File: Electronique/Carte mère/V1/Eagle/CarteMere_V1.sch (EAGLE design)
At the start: 25 parts, among them J100 BP_Rouge, J101 BP Jaune, J102 BP Vert, J600 LED_VERTE, J601 LED_JAUNE, J602 LED_ROUGE, Q500 SI2303DS, Q501 SI2302DS, U200 FIREBEETLE-ESP32-DFR0478, U300 RTC_ADA-3295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

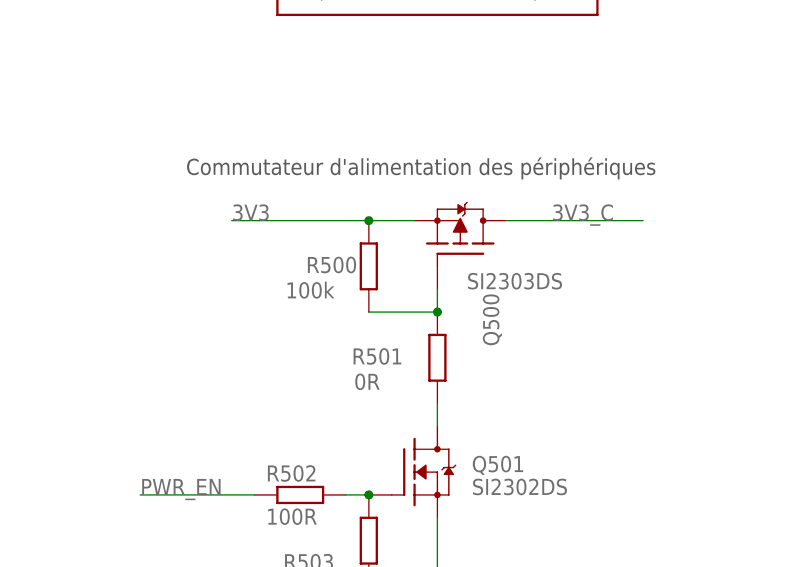
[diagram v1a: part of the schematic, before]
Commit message: Modificaiton du diamètre perçage vis et recréation des fichiers gerbers
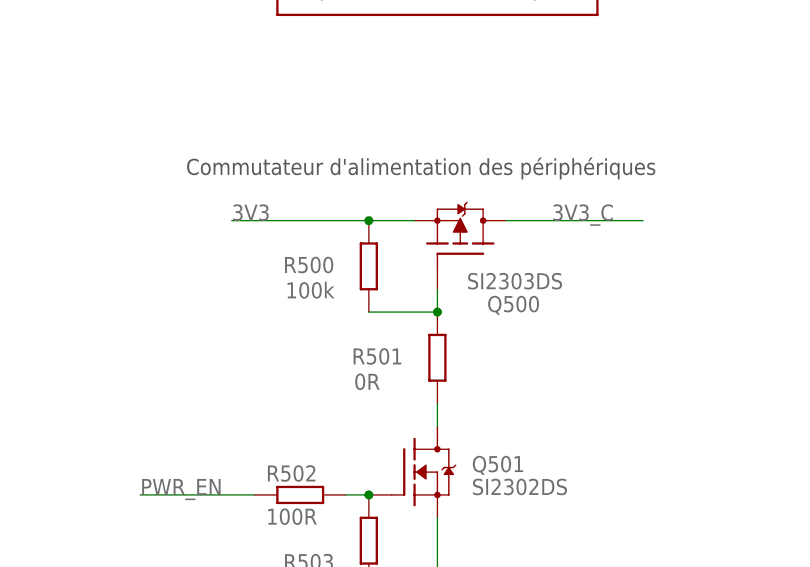
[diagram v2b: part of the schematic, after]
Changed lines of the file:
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@@
 <part name="SUPPLY3" library="supply2" library_urn="urn:adsk.eagle:library:372" deviceset="GND" device=""/>
 <part name="SUPPLY4" library="supply2" library_urn="urn:adsk.eagle:library:372" deviceset="GND" device=""/>
-<part name="R501" library="Eagle_UOF_Lib" deviceset="R_1/4W" device="10" value="0R"/>
-<part name="R500" library="Eagle_UOF_Lib" deviceset="R_1/4W" device="10" value="100k"/>
 <part name="Q500" library="Eagle_UOF_Lib" deviceset="SI2303DS" device=""/>
 <part name="JTEST300" library="pinhead" library_urn="urn:adsk.eagle:library:325" deviceset="PINHD-1X1" device="" package3d_urn="urn:adsk.eagle:package:22485/1"/>
@@
 <part name="JTEST400" library="pinhead" library_urn="urn:adsk.eagle:library:325" deviceset="PINHD-1X1" device="" package3d_urn="urn:adsk.eagle:package:22485/1"/>
 <part name="JTEST401" library="pinhead" library_urn="urn:adsk.eagle:library:325" deviceset="PINHD-1X1" device="" package3d_urn="urn:adsk.eagle:package:22485/1"/>
+<part name="R501" library="Eagle_UOF_Lib" deviceset="R_1/4W" device="10" value="0R"/>
+<part name="R500" library="Eagle_UOF_Lib" deviceset="R_1/4W" device="10" value="100k"/>
 </parts>
 <sheets>
@@
 <instance part="SUPPLY3" gate="GND" x="137.16" y="20.32"/>
 <instance part="SUPPLY4" gate="GND" x="137.16" y="5.08"/>
-<instance part="R501" gate="G$1" x="73.66" y="0" smashed="yes" rot="R90">
-<attribute name="NAME" x="69.85" y="1.0414" size="1.778" layer="95" rot="R180"/>
-<attribute name="VALUE" x="67.31" y="-1.778" size="1.778" layer="96" rot="R180"/>
-</instance>
-<instance part="R500" gate="G$1" x="66.04" y="10.16" smashed="yes" rot="R90">
-<attribute name="NAME" x="64.77" y="11.2014" size="1.778" layer="95" rot="R180"/>
-<attribute name="VALUE" x="62.23" y="8.382" size="1.778" layer="96" rot="R180"/>
-</instance>
 <instance part="Q500" gate="G$1" x="76.2" y="12.7" smashed="yes" rot="MR90">
 <attribute name="VALUE" x="87.63" y="7.62" size="1.778" layer="96" rot="MR0"/>
-<attribute name="NAME" x="78.74" y="1.27" size="1.778" layer="95" rot="MR90"/>
+<attribute name="NAME" x="85.09" y="5.08" size="1.778" layer="95" rot="MR0"/>
 </instance>
 <instance part="JTEST300" gate="G$1" x="17.78" y="-25.4" rot="R90"/>
@@
 <instance part="JTEST400" gate="G$1" x="132.08" y="86.36" rot="R90"/>
 <instance part="JTEST401" gate="G$1" x="124.46" y="86.36" rot="R90"/>
+<instance part="R501" gate="G$1" x="73.66" y="0" smashed="yes" rot="R90">
+<attribute name="NAME" x="69.85" y="1.0414" size="1.778" layer="95" rot="R180"/>
+<attribute name="VALUE" x="67.31" y="-1.778" size="1.778" layer="96" rot="R180"/>
+</instance>
+<instance part="R500" gate="G$1" x="66.04" y="10.16" smashed="yes" rot="R90">
+<attribute name="NAME" x="62.23" y="11.2014" size="1.778" layer="95" rot="R180"/>
+<attribute name="VALUE" x="62.23" y="8.382" size="1.778" layer="96" rot="R180"/>
+</instance>
 </instances>
 <busses>
@@
 </segment>
 <segment>
+<wire x1="71.12" y1="15.24" x2="66.04" y2="15.24" width="0.1524" layer="91"/>
+<label x="50.8" y="15.24" size="1.778" layer="95"/>
+<pinref part="Q500" gate="G$1" pin="S"/>
 <pinref part="R500" gate="G$1" pin="2"/>
 <wire x1="66.04" y1="15.24" x2="50.8" y2="15.24" width="0.1524" layer="91"/>
-<label x="50.8" y="15.24" size="1.778" layer="95"/>
-<pinref part="Q500" gate="G$1" pin="S"/>
-<wire x1="66.04" y1="15.24" x2="71.12" y2="15.24" width="0.1524" layer="91"/>
 <junction x="66.04" y="15.24"/>
 </segment>
@@
 <net name="N$7" class="0">
 <segment>
-<pinref part="R501" gate="G$1" pin="2"/>
-<pinref part="R500" gate="G$1" pin="1"/>
 <wire x1="66.04" y1="5.08" x2="73.66" y2="5.08" width="0.1524" layer="91"/>
 <pinref part="Q500" gate="G$1" pin="G"/>
 <wire x1="73.66" y1="7.62" x2="73.66" y2="5.08" width="0.1524" layer="91"/>
+<pinref part="R501" gate="G$1" pin="2"/>
 <junction x="73.66" y="5.08"/>
-</segment>
-</net>
+<pinref part="R500" gate="G$1" pin="1"/>
+</segment>
+</net>
